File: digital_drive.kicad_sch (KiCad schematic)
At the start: 20 parts, among them Q1501 MMBT3904L, Q1502 MMBT3904L, Q1503 MMBT3904L, U1501 EPC23104ENGRT, U1502 EPC23104ENGRT

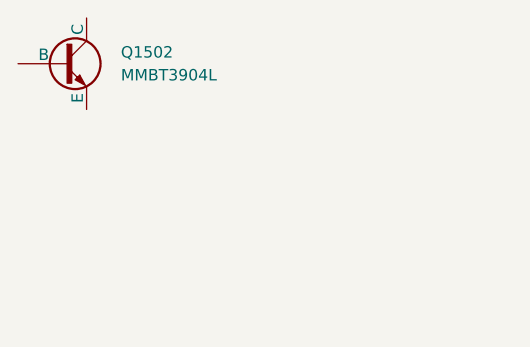
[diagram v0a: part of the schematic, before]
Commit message: subcircuit layout + minor schematic updates
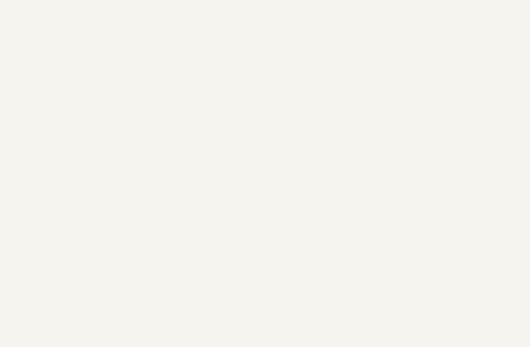
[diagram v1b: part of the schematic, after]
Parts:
- removed Q1502: MMBT3904L, BR_SOT:SOT-23, symbol BR_Transistors:BJT_N_MMBT3904L
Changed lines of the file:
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@@
-		)
-	)
-	(symbol
-		(lib_id "BR_Transistors:BJT_N_MMBT3904L")
-		(at -11818.62 -6525.26 0)
-		(unit 1)
-		(exclude_from_sim no)
-		(in_bom yes)
-		(on_board yes)
-		(dnp no)
-		(fields_autoplaced yes)
-		(property "Reference" "Q1502"
-			(at -11812.27 -6526.5301 0)
-			(effects
-				(font
-					(size 1.27 1.27)
-				)
-				(justify left)
-			)
-		)
-		(property "Value" "MMBT3904L"
-			(at -11812.27 -6523.9901 0)
-			(effects
-				(font
-					(size 1.27 1.27)
-				)
-				(justify left)
-			)
-		)
-		(property "Footprint" "BR_SOT:SOT-23"
-			(at -11818.62 -6601.46 0)
-			(effects
-				(font
-					(size 1.27 1.27)
-				)
-				(justify left)
-				(hide yes)
-			)
-		)
-		(property "Datasheet" "https://www.onsemi.com/pdf/datasheet/mmbt3904lt1-d.pdf"
-			(at -11818.62 -6598.92 0)
-			(effects
-				(font
-					(size 1.27 1.27)
-				)
-				(justify left)
-				(hide yes)
-			)
-		)
-		(property "Description" "NPN BJT 40V 200mA 300mW 300MHz SOT-23-3"
-			(at -11818.62 -6588.76 0)
-			(effects
-				(font
-					(size 1.27 1.27)
-				)
-				(justify left)
-				(hide yes)
-			)
-		)
-		(property "Manufacturer" "onsemi"
-			(at -11818.62 -6596.38 0)
-			(effects
-				(font
-					(size 1.27 1.27)
-				)
-				(justify left)
-				(hide yes)
-			)
-		)
-		(property "Manufacturer Part Num" "MMBT3904LT1G"
-			(at -11818.62 -6593.84 0)
-			(effects
-				(font
-					(size 1.27 1.27)
-				)
-				(justify left)
-				(hide yes)
-			)
-		)
-		(property "BRE Number" "BRE-000400"
-			(at -11818.62 -6591.3 0)
-			(effects
-				(font
-					(size 1.27 1.27)
-				)
-				(justify left)
-				(hide yes)
-			)
-		)
-		(property "Supplier 1" "DigiKey"
-			(at -11818.62 -6586.22 0)
-			(effects
-				(font
-					(size 1.27 1.27)
-				)
-				(justify left)
-				(hide yes)
-			)
-		)
-		(property "Supplier Part Num 1" "MMBT3904LT1GOSCT-ND"
-			(at -11818.62 -6583.68 0)
-			(effects
-				(font
-					(size 1.27 1.27)
-				)
-				(justify left)
-				(hide yes)
-			)
-		)
-		(property "Supplier 2" "DigiKey"
-			(at -11818.62 -6581.14 0)
-			(effects
-				(font
-					(size 1.27 1.27)
-				)
-				(justify left)
-				(hide yes)
-			)
-		)
-		(property "Supplier Part Num 2" "MMBT3904LT1GOSTR-ND"
-			(at -11818.62 -6578.6 0)
-			(effects
-				(font
-					(size 1.27 1.27)
-				)
-				(justify left)
-				(hide yes)
-			)
-		)
-		(property "Supplier 3" "JLCPCB"
-			(at -11818.62 -6576.06 0)
-			(effects
-				(font
-					(size 1.27 1.27)
-				)
-				(justify left)
-				(hide yes)
-			)
-		)
-		(property "Supplier Part Num 3" "C81464/ C84555"
-			(at -11818.62 -6573.52 0)
-			(effects
-				(font
-					(size 1.27 1.27)
-				)
-				(justify left)
-				(hide yes)
-			)
-		)
-		(property "JLCPCB Part Num" "C81464"
-			(at -11818.62 -6565.9 0)
-			(effects
-				(font
-					(size 1.27 1.27)
-				)
-				(justify left)
-				(hide yes)
-			)
-		)
-		(pin "3"
-		)
-		(pin "2"
-		)
-		(pin "1"
-		)
-		(instances
-			(project ""
-				(path "/2a5ce3ef-537a-4122-a1be-ef76186bc0d7/e1c72b00-0544-40b2-bdd8-a4cf7df3ac65/1e5859a0-f8d4-4fa9-a838-2018b8a35fcb"
-					(reference "Q1502")
-					(unit 1)
-				)
-			)
 		)
 	)

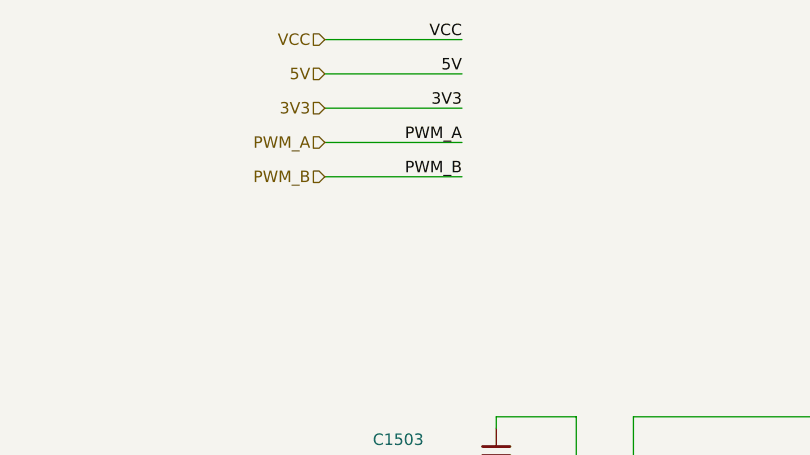
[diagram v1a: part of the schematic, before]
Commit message: more test points+ routing improvements
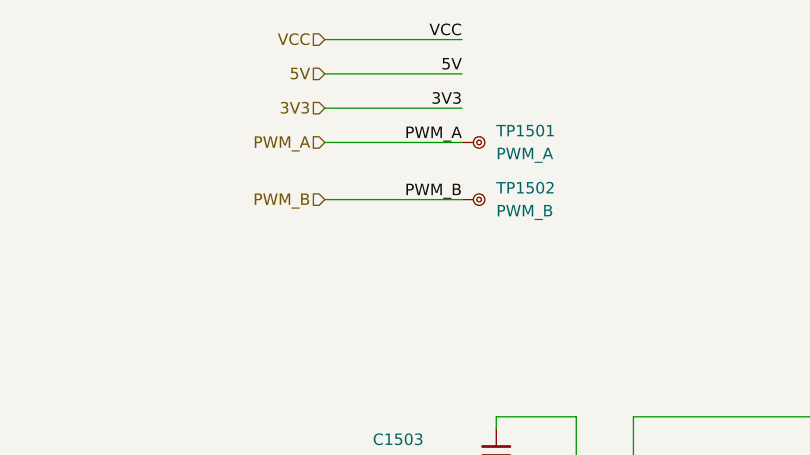
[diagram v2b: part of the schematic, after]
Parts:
- added TP1501: PWM_A, BR_Connectors:TEST-TH_BD2.54-P1.4_RED, symbol BR_Connectors:TP_Ring_PTH
- added TP1502: PWM_B, BR_Connectors:TEST-TH_BD2.54-P1.4_RED, symbol BR_Connectors:TP_Ring_PTH
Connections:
- net PWM_A: now also TP1501.1
- net PWM_B: now also TP1502.1

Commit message: preboard review of updates
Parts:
- removed Q1501, Q1503: MMBT3904L, BR_SOT:SOT-23, symbol BR_Transistors:BJT_N_MMBT3904L
- removed R1501, R1508: 24k9, BR_Passives:C_0402_1005Metric-minimized, symbol BR_Resistors_0402:R_0402_24k9
- removed R1506, R1507: 5k1, BR_Passives:C_0402_1005Metric-minimized, symbol BR_Resistors_0402:R_0402_5k1
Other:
- moved on the sheet: TP1501, TP1502

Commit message: various improvements
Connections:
- net VCC renamed VTX
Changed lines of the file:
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@@
+	(wire
+		(pts
+			(xy 77.47 55.88) (xy 92.71 55.88)
+		)
+		(stroke
+			(width 0)
+			(type default)
+		)
+	)
 	(wire
 		(pts
@@
 		)
 	)
-	(label "VCC"
+	(label "VTX"
 		(at 149.86 76.2 180)
 		(effects
@@
 		)
 	)
+	(label "GND"
+		(at 92.71 55.88 180)
+		(effects
+			(font
+				(size 1.27 1.27)
+			)
+			(justify right bottom)
+		)
+	)
 	(label "5V"
 		(at 62.23 92.71 0)
@@
 		)
 	)
-	(label "VCC"
+	(label "VTX"
 		(at 92.71 38.1 180)
 		(effects
@@
 		)
 	)
+	(hierarchical_label "GND"
+		(shape input)
+		(at 77.47 55.88 180)
+		(effects
+			(font
+				(size 1.27 1.27)
+			)
+			(justify right)
+		)
+	)
 	(hierarchical_label "5V"
 		(shape input)
@@
 		)
 	)
-	(hierarchical_label "VCC"
+	(hierarchical_label "VTX"
 		(shape input)
 		(at 77.47 38.1 180)

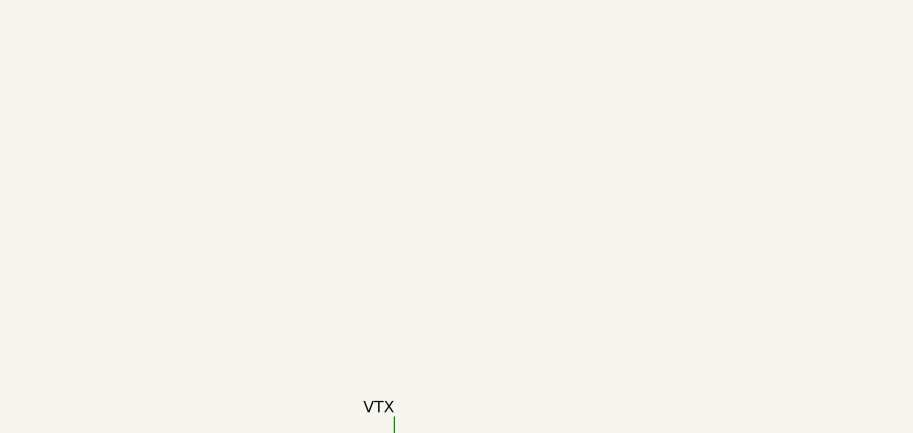
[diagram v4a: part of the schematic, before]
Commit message: added RC filters on RX power + new TIM8 pins
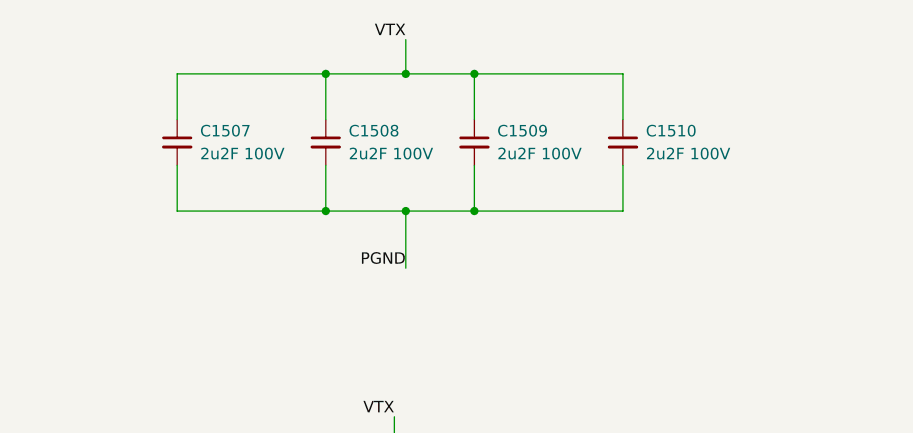
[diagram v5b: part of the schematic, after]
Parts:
- added C1507, C1508, C1509, C1510: 2u2F 100V, BR_Passives:C_0805_2012Metric-minimized, symbol BR_Capacitors_0805:C_0805_2u2F_100V_X7T_10%
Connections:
- net PGND: now also C1507.2, C1508.2, C1509.2, C1510.2
- net VTX: now also C1507.1, C1508.1, C1509.1, C1510.1

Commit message: last checks + board characteristics tables
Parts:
- NT1501: footprint BR_Virtual_Parts:NetTie-2_SMD_Pad_0.18mm_wide_long -> BR_Virtual_Parts:NetTie-2_SMD_Pad_3.88mm_wide; symbol BR_Virtual_Parts:NetTie-2_0.18mm_long -> BR_Virtual_Parts:NetTie-2_3.88mm
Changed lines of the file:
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@@
 	)
 	(symbol
-		(lib_id "BR_Virtual_Parts:NetTie-2_0.18mm_long")
+		(lib_id "BR_Virtual_Parts:NetTie-2_3.88mm")
 		(at 149.86 154.94 90)
 		(unit 1)
-		(exclude_from_sim no)
+		(exclude_from_sim yes)
 		(in_bom no)
 		(on_board yes)
@@
 		)
 		(property "Value" "NetTie-2_0.18mm"
-			(at 149.86 151.765 90)
+			(at 149.86 152.4 90)
 			(effects
 				(font
@@
 			)
 		)
-		(property "Footprint" "BR_Virtual_Parts:NetTie-2_SMD_Pad_0.18mm_wide_long"
-			(at 150.114 153.924 90)
+		(property "Footprint" "BR_Virtual_Parts:NetTie-2_SMD_Pad_3.88mm_wide"
+			(at 149.86 154.94 0)
 			(effects
 				(font
@@
 		)
 		(property "Datasheet" "~"
-			(at 144.78 146.05 0)
+			(at 149.86 154.94 0)
 			(effects
 				(font
@@
 		)
 		(property "Manufacturer" "~"
-			(at 130.81 152.4 0)
+			(at 149.86 154.94 0)
 			(effects
 				(font
 					(size 1.27 1.27)
 				)
-				(justify left)
 				(hide yes)
 			)
 		)
 		(property "Supplier 1" "~"
-			(at 128.27 152.4 0)
+			(at 149.86 154.94 0)
 			(effects
 				(font
 					(size 1.27 1.27)
 				)
-				(justify left)
 				(hide yes)
 			)
 		)
 		(property "Supplier Part Num 1" "~"
-			(at 125.73 152.4 0)
+			(at 149.86 154.94 0)
 			(effects
 				(font
 					(size 1.27 1.27)
 				)
-				(justify left)
 				(hide yes)
 			)
 		)
 		(property "Supplier 2" "~"
-			(at 123.19 152.4 0)
+			(at 149.86 154.94 0)
 			(effects
 				(font
 					(size 1.27 1.27)
 				)
-				(justify left)
 				(hide yes)
 			)
 		)
 		(property "Supplier Part Num 2" "~"
-			(at 120.65 152.4 0)
+			(at 149.86 154.94 0)
 			(effects
 				(font
 					(size 1.27 1.27)
 				)
-				(justify left)
 				(hide yes)
 			)
 		)
 		(property "Supplier 3" "~"
-			(at 118.11 152.4 0)
+			(at 149.86 154.94 0)
 			(effects
 				(font
 					(size 1.27 1.27)
 				)
-				(justify left)
 				(hide yes)
 			)
 		)
 		(property "Supplier Part Num 3" "~"
-			(at 115.57 152.4 0)
+			(at 149.86 154.94 0)
 			(effects
 				(font
 					(size 1.27 1.27)
 				)
-				(justify left)
 				(hide yes)
 			)
 		)
 		(property "Manufacturer Part Num" "~"
-			(at 113.03 152.4 0)
+			(at 149.86 154.94 0)
 			(effects
 				(font
 					(size 1.27 1.27)
 				)
-				(justify left)
 				(hide yes)
 			)

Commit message: Rev A release files
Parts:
- C1501, C1506: JLCPCB Part Num C528974 -> C23692972
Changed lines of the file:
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@@
 			)
 		)
-		(property "JLCPCB Part Num" "C528974"
+		(property "JLCPCB Part Num" "C23692972"
 			(at 231.14 50.8 0)
 			(effects
@@
 	)
 	(symbol
-		(lib_name "EPC23104ENGRT_1")
 		(lib_id "BR_PMIC:EPC23104ENGRT")
 		(at 105.41 104.14 0)
@@
 			)
 		)
-		(property "JLCPCB Part Num" "C528974"
+		(property "JLCPCB Part Num" "C23692972"
 			(at 67.31 50.8 0)
 			(effects
